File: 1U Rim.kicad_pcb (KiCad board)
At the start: 2 copper layers, 56.9 x 28.7 mm, 71 parts, among them J1 Trigger, J10 POT_M, J2 Accent, J3 PWR, J4 Out, J5 PWR_C, J6 PWR_M, J7 JCK_C, J8 JCK_M, J9 POT_C, Q1 BC849, Q2 BC859, Q3 BC849, U1 TL074, U2 TL072

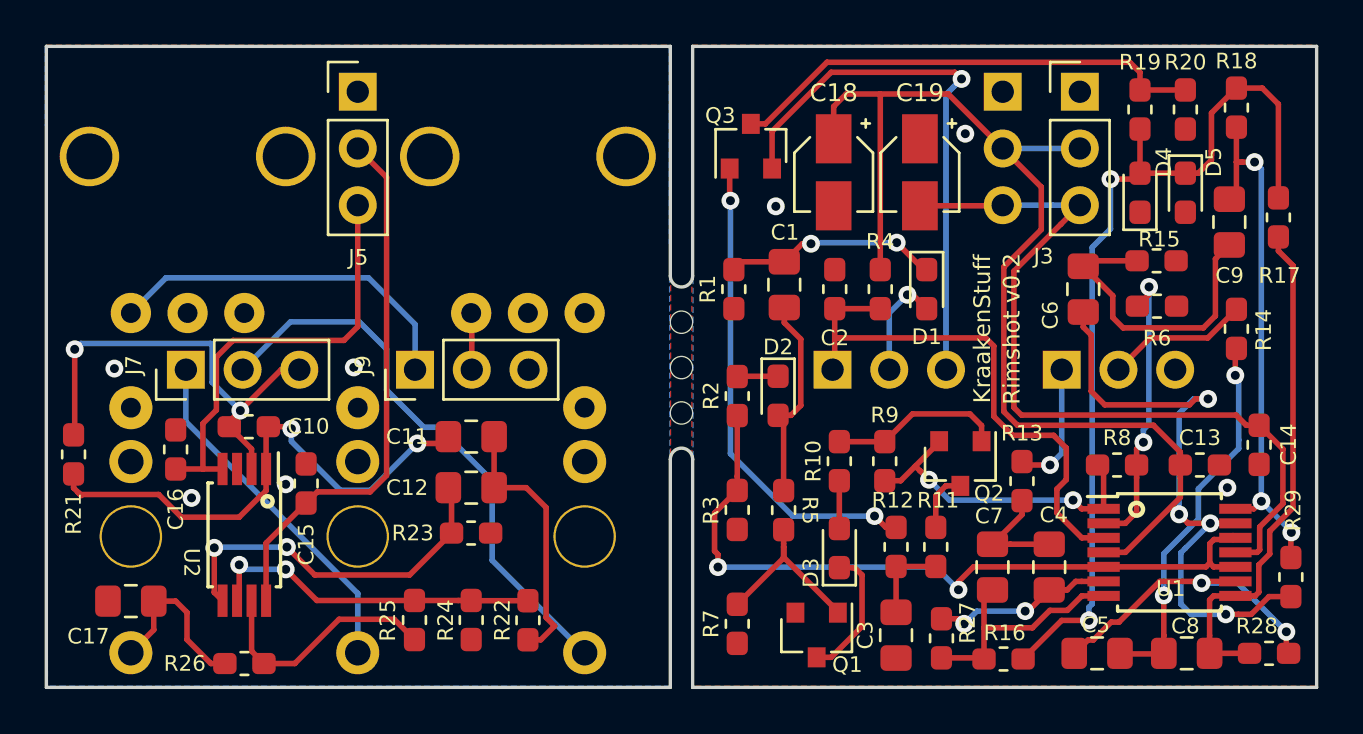
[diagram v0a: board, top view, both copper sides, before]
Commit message: Added a new handling for Accent
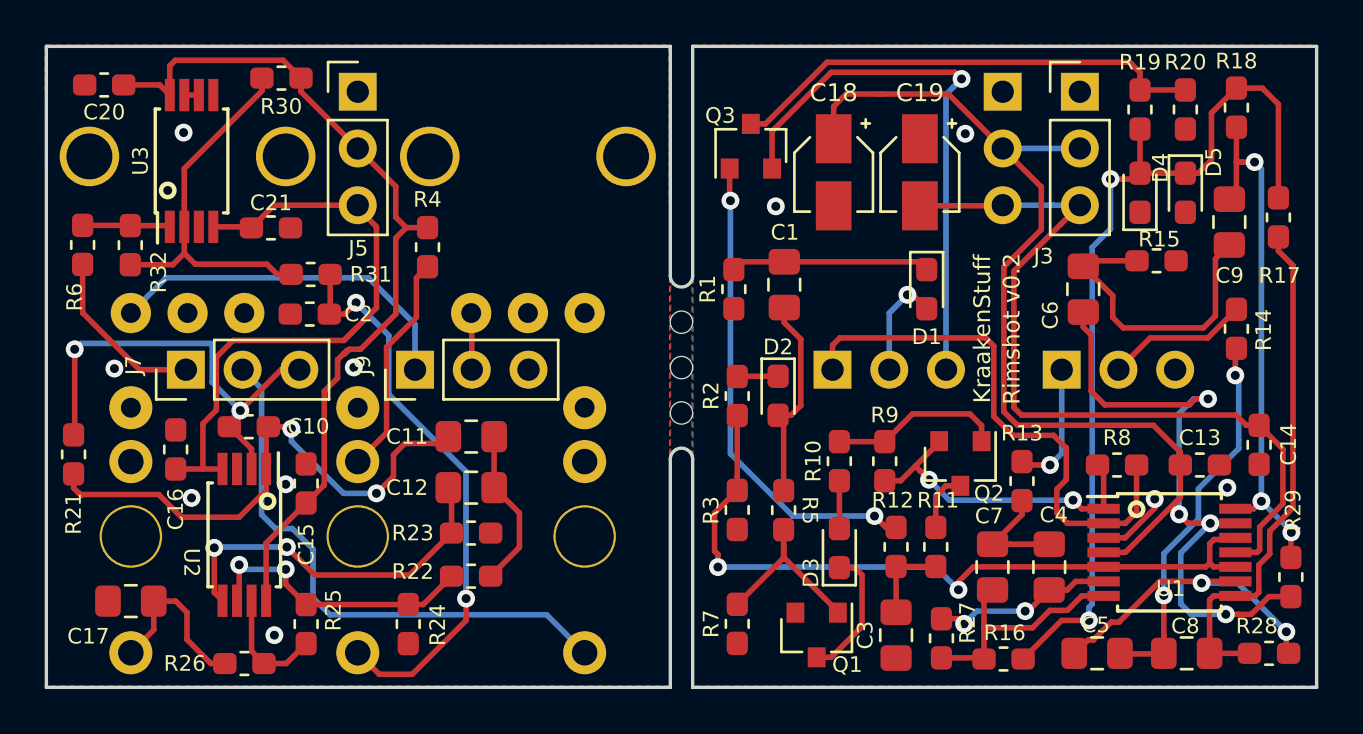
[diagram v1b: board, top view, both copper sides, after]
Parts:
- added C20: 100n, Capacitor_SMD:C_0603_1608Metric_Pad1.05x0.95mm_HandSolder, F.Cu at (22.7, 23.4)
- added C21: 100n, Capacitor_SMD:C_0603_1608Metric_Pad1.05x0.95mm_HandSolder, F.Cu at (30.2, 29.8)
- added R30: 180k, Resistor_SMD:R_0603_1608Metric_Pad1.05x0.95mm_HandSolder, F.Cu at (30.6, 23.1)
- added R31: 100k, Resistor_SMD:R_0603_1608Metric_Pad1.05x0.95mm_HandSolder, F.Cu at (32.0, 31.9)
- added R32: 100k, Resistor_SMD:R_0603_1608Metric_Pad1.05x0.95mm_HandSolder, F.Cu at (23.9, 30.5)
- added U3: TL072, Package_SO:TSSOP-8_4.4x3mm_P0.65mm, F.Cu at (26.6, 26.8)
- R6: value 4.7k -> 100k
- R8: value 10k -> 100k
- moved R6 48.2 mm to (21.7, 30.5), turned to 90 degrees
- moved C2 23.5 mm to (31.9, 33.6), turned to 180 degrees
- moved R4 20.4 mm to (37.2, 30.6)
- moved R25 4.85 mm to (31.8, 47.5)
- moved R22 3.22 mm to (39.1, 45.4), turned to 0 degrees
- moved R24 2.83 mm to (36.3, 47.5)
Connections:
- C2 pad 1: Acc -> Net-(C2-Pad1)
- J2 pad T: Acc -> Net-(C2-Pad1)
- R4 pad 2: Acc -> Net-(J2-PadTN)
- R6 pad 1: GND -> Acc
- R6 pad 2: Net-(R6-Pad2) -> Net-(R32-Pad2)
- R8 pad 2: Net-(R6-Pad2) -> Acc
- U1 pad 2: Net-(R6-Pad2) -> Acc
- U1 pad 3: Acc -> GND
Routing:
- net Net-(C2-Pad1): track 0.00 -> 25.7 mm, vias 0 -> 2
- net Net-(R30-Pad2): track 0.00 -> 17.1 mm
- net Net-(R6-Pad2): track 13.1 -> 0.00 mm, vias 2 -> 0
- net Net-(J2-PadTN): track 0.00 -> 10.0 mm
- net -12V: track 56.0 -> 64.5 mm
- net Acc: track 40.6 -> 32.7 mm
- net +12V: track 74.3 -> 81.4 mm
- net Net-(R25-Pad1): track 11.0 -> 5.30 mm
- net Net-(C11-Pad1): track 11.9 -> 7.25 mm
- net Net-(R32-Pad2): track 0.00 -> 3.93 mm
- net GND: track 0.00 -> 3.25 mm, vias 7 -> 10
- net Net-(R22-Pad1): track 15.2 -> 12.8 mm
- net Net-(C1-Pad2): track 9.64 -> 8.93 mm, vias 2 -> 0
- net Net-(C10-Pad1): track 24.0 -> 24.6 mm
- net Net-(U3-Pad6): track 0.00 -> 0.65 mm
